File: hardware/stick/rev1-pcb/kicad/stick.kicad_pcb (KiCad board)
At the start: 4 copper layers, 60 x 30 mm, 13 parts, among them J1 USB4135-GF-A, J2 GDEY0154D67, J3 Nano-SIM Push-Push, SW1 BTN_L, SW2 BTN_R, U1 IP4292CZ12, U2 TPS2553, U3 AP2112K-3.3, U4 nRF52840, Y1 32MHz, Y2 32.768kHz

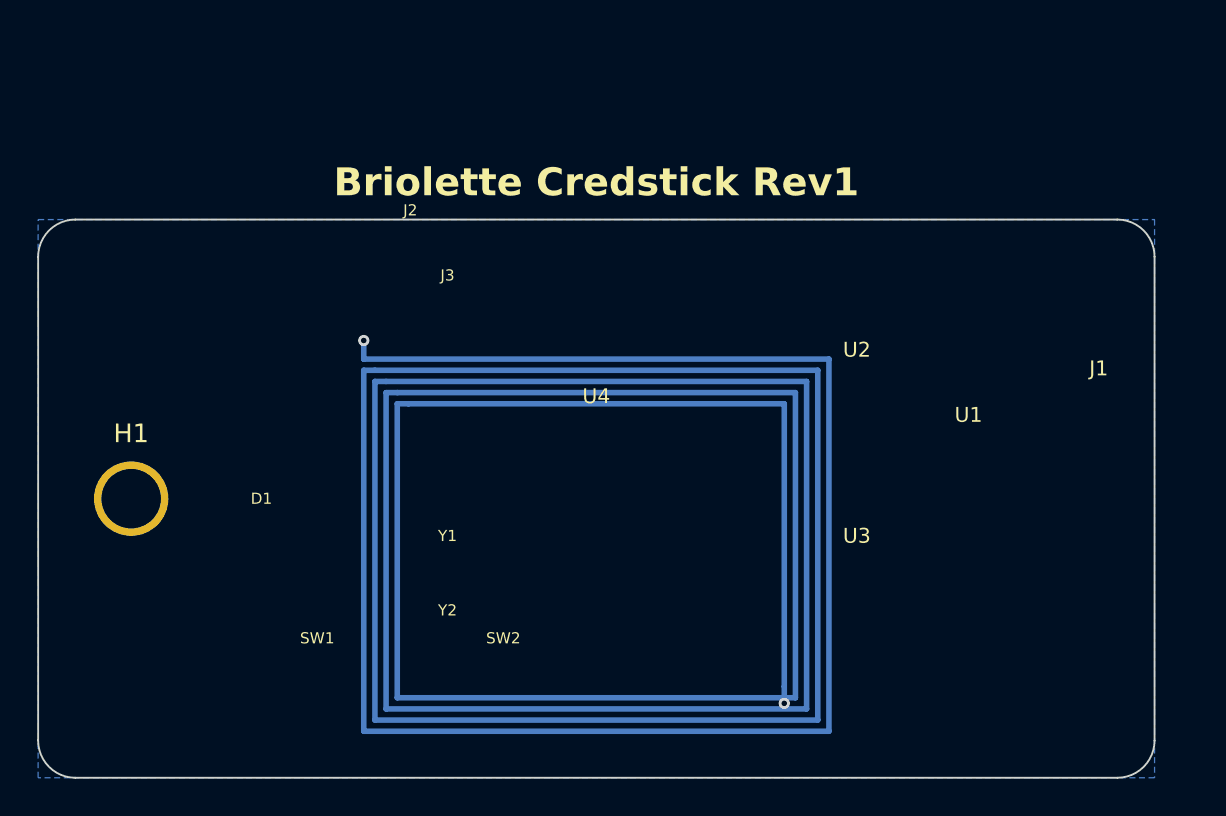
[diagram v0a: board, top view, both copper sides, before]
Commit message: Add missing passive footprints, fix firmware pin assignments
PCB changes (both boards):
- Add pad definitions to all footprints from library .kicad_mod files
- Add all missing passive components: decoupling caps, crystal load
  caps, LDO bypass caps, NFC matching network, pull-up/pull-down
  resistors, LED, piezo buffer cap, supercapacitor footprints
- Stick: 12 → 24 unique BOM parts on PCB
- Relay: 22 → 43 unique BOM parts on PCB

Firmware fixes:
- Stick: Realign display pins to match schematic (P0.15=CS, P0.16=DC,
  P0.17=RST, P0.18=BUSY), add TODO for SPIM peripheral init
- Relay: Add KEY_INT (P0.09) and KEY_RST (P0.10) pin definitions for
  TCA8418 keypad scanner, add TODO for I2C bus sharing

Docs:
- Update power-analysis.md: replace ATECC608B references with SIM card

Co-Authored-By: Claude Opus 4.6 (1M context) <noreply@anthropic.com>
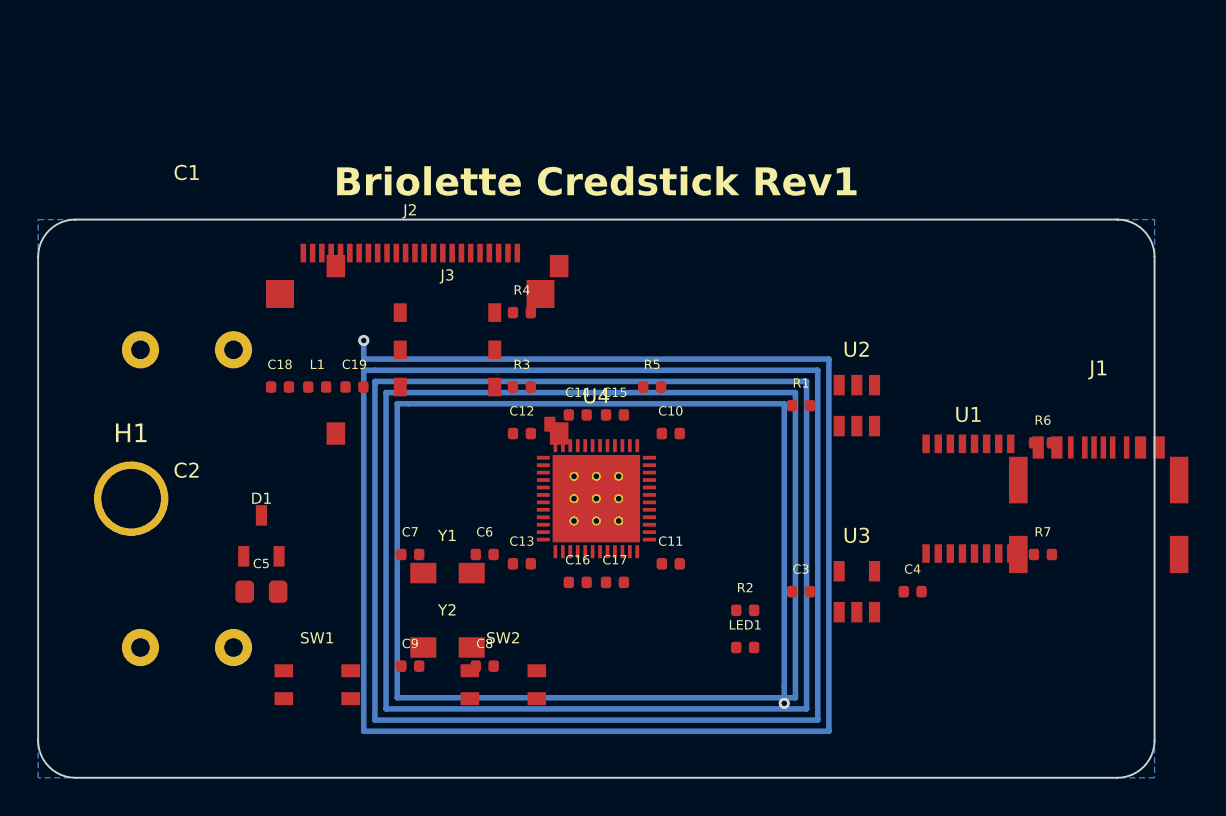
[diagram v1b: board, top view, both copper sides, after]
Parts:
- added C1: 5F 3V, stick-lib:Supercap_Cylindrical_14mm, F.Cu at (-22.0, -8.00)
- added C10: 100nF, Capacitor_SMD:C_0402_1005Metric, F.Cu at (4.00, -3.50)
- added C11: 100nF, Capacitor_SMD:C_0402_1005Metric, F.Cu at (4.00, 3.50)
- added C12: 100nF, Capacitor_SMD:C_0402_1005Metric, F.Cu at (-4.00, -3.50)
- added C13: 100nF, Capacitor_SMD:C_0402_1005Metric, F.Cu at (-4.00, 3.50)
- added C14: 100nF, Capacitor_SMD:C_0402_1005Metric, F.Cu at (-1.00, -4.50)
- added C15: 100nF, Capacitor_SMD:C_0402_1005Metric, F.Cu at (1.00, -4.50)
- added C16: 100nF, Capacitor_SMD:C_0402_1005Metric, F.Cu at (-1.00, 4.50)
- added C17: 100nF, Capacitor_SMD:C_0402_1005Metric, F.Cu at (1.00, 4.50)
- added C18: 180pF, Capacitor_SMD:C_0402_1005Metric, F.Cu at (-17.0, -6.00)
- added C19: 180pF, Capacitor_SMD:C_0402_1005Metric, F.Cu at (-13.0, -6.00)
- added C2: 5F 3V, stick-lib:Supercap_Cylindrical_14mm, F.Cu at (-22.0, 8.00)
- added C3: 10uF, Capacitor_SMD:C_0402_1005Metric, F.Cu at (11.0, 5.00)
- added C4: 10uF, Capacitor_SMD:C_0402_1005Metric, F.Cu at (17.0, 5.00)
- added C5: 100uF, Capacitor_SMD:C_0805_2012Metric, F.Cu at (-18.0, 5.00)
- added C6: 12pF, Capacitor_SMD:C_0402_1005Metric, F.Cu at (-6.00, 3.00)
- added C7: 12pF, Capacitor_SMD:C_0402_1005Metric, F.Cu at (-10.0, 3.00)
- added C8: 6.8pF, Capacitor_SMD:C_0402_1005Metric, F.Cu at (-6.00, 9.00)
- added C9: 6.8pF, Capacitor_SMD:C_0402_1005Metric, F.Cu at (-10.0, 9.00)
- added L1: 390nH, Inductor_SMD:L_0402_1005Metric, F.Cu at (-15.0, -6.00)
- added LED1: Green, LED_SMD:LED_0402_1005Metric, F.Cu at (8.00, 8.00)
- added R1: 10k, Resistor_SMD:R_0402_1005Metric, F.Cu at (11.0, -5.00)
- added R2: 1k, Resistor_SMD:R_0402_1005Metric, F.Cu at (8.00, 6.00)
- added R3: 10k, Resistor_SMD:R_0402_1005Metric, F.Cu at (-4.00, -6.00)
- added R4: 10k, Resistor_SMD:R_0402_1005Metric, F.Cu at (-4.00, -10.0)
- added R5: 10k, Resistor_SMD:R_0402_1005Metric, F.Cu at (3.00, -6.00)
- added R6: 5.1k, Resistor_SMD:R_0402_1005Metric, F.Cu at (24.0, -3.00)
- added R7: 5.1k, Resistor_SMD:R_0402_1005Metric, F.Cu at (24.0, 3.00)

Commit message: Fix pre-fabrication review issues on both PCBs
Stick:
- Add piezo harvester footprint (J4, Piezo_Cantilever_25x5mm)
- Add NFC_ANT2 return trace on F.Cu from antenna exit via back to
  matching network area
- Fix 32MHz crystal footprint: 3215 (3.2x1.5mm) -> 3225 (3.2x2.5mm)
  to match ABM8 package

Relay:
- Add 5 missing components: BAT54S rectifier (D1), IP4292CZ12 ESD
  protection (U6), TPS2553 charge limiter (U7), solar cell pads (J2),
  piezo harvester (J3)
- Add both crystals: Y1 (32MHz, 3225 package) and Y2 (32.768kHz, 3215)
- Replace BQ25504 inductor L2 from 0402 to Coilcraft LPS4018 (4x4mm)
  matching the BQ25504 datasheet requirement
- Add missing 3rd 10uF bulk cap (C33)

Co-Authored-By: Claude Opus 4.6 (1M context) <noreply@anthropic.com>
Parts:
- added J4: PPA-1014, stick-lib:Piezo_Cantilever_25x5mm, F.Cu at (-20.0, -12.0)
- Y1: footprint Crystal:Crystal_SMD_3215-2Pin_3.2x1.5mm -> Crystal:Crystal_SMD_3225-2Pin_3.2x2.5mm
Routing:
- net NFC_ANT2: track 0.00 -> 44.1 mm
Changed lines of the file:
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@@
     (pad "SH" smd rect (at 6.0 4.5) (size 1.0 1.2) (layers "F.Cu" "F.Paste" "F.Mask") (uuid "fp-nsim-sh-004") )
   )
-  (footprint "Crystal:Crystal_SMD_3215-2Pin_3.2x1.5mm"
+  (footprint "Crystal:Crystal_SMD_3225-2Pin_3.2x2.5mm"
     (layer "F.Cu")
     (at -8.0 4.0 0)
@@
     (pad "2" thru_hole circle (at 2.5 0) (size 2.0 2.0) (drill 1.0) (layers "*.Cu" "*.Mask"))
   )
+  (footprint "stick-lib:Piezo_Cantilever_25x5mm"
+    (layer "F.Cu")
+    (at -20.0 -12.0 90)
+    (property "Reference" "J4"
+      (at 0 -5.0 0)
+      (layer "F.SilkS")
+      (effects (font (size 0.6 0.6) (thickness 0.1)))
+    )
+    (property "Value" "PPA-1014"
+      (at 0 5.0 0)
+      (layer "F.Fab")
+      (effects (font (size 0.6 0.6) (thickness 0.1)))
+    )
+    (pad "1" smd rect (at 11.0 -1.5) (size 2.0 1.5) (layers "F.Cu" "F.Paste" "F.Mask"))
+    (pad "2" smd rect (at 11.0 1.5) (size 2.0 1.5) (layers "F.Cu" "F.Paste" "F.Mask"))
+    (pad "MP" thru_hole circle (at 12.0 0) (size 1.6 1.6) (drill 1.0) (layers "*.Cu" "*.Mask"))
+  )
+  (segment (start 10.1 11.0) (end 10.1 13.0) (width 0.3) (layer "F.Cu") (net 25))
+  (segment (start 10.1 13.0) (end -13.0 13.0) (width 0.3) (layer "F.Cu") (net 25))
+  (segment (start -13.0 13.0) (end -13.0 -6.0) (width 0.3) (layer "F.Cu") (net 25))
 )
